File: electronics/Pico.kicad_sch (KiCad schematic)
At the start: 36 parts, among them J1 USB_B_Micro, SW1 PTS645SK50SMTR92LFS, U1 W25Q32JVZP, U2 RP2040, Y1 Crystal

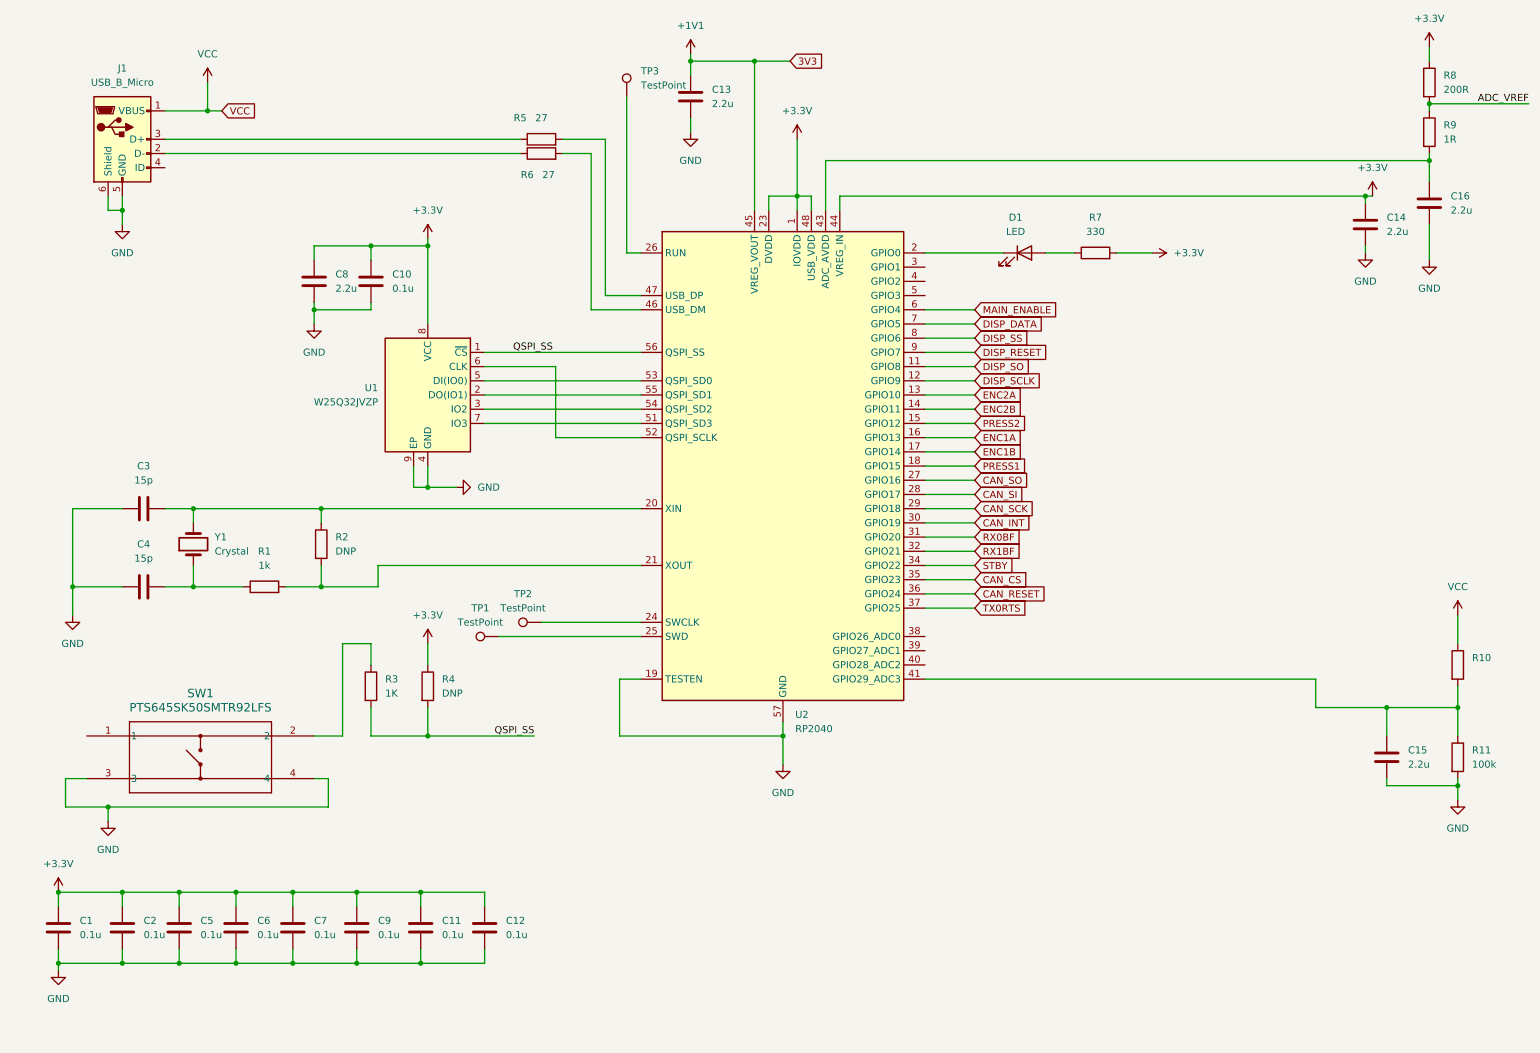
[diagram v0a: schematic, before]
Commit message: Many changes to the design. Fully routed.
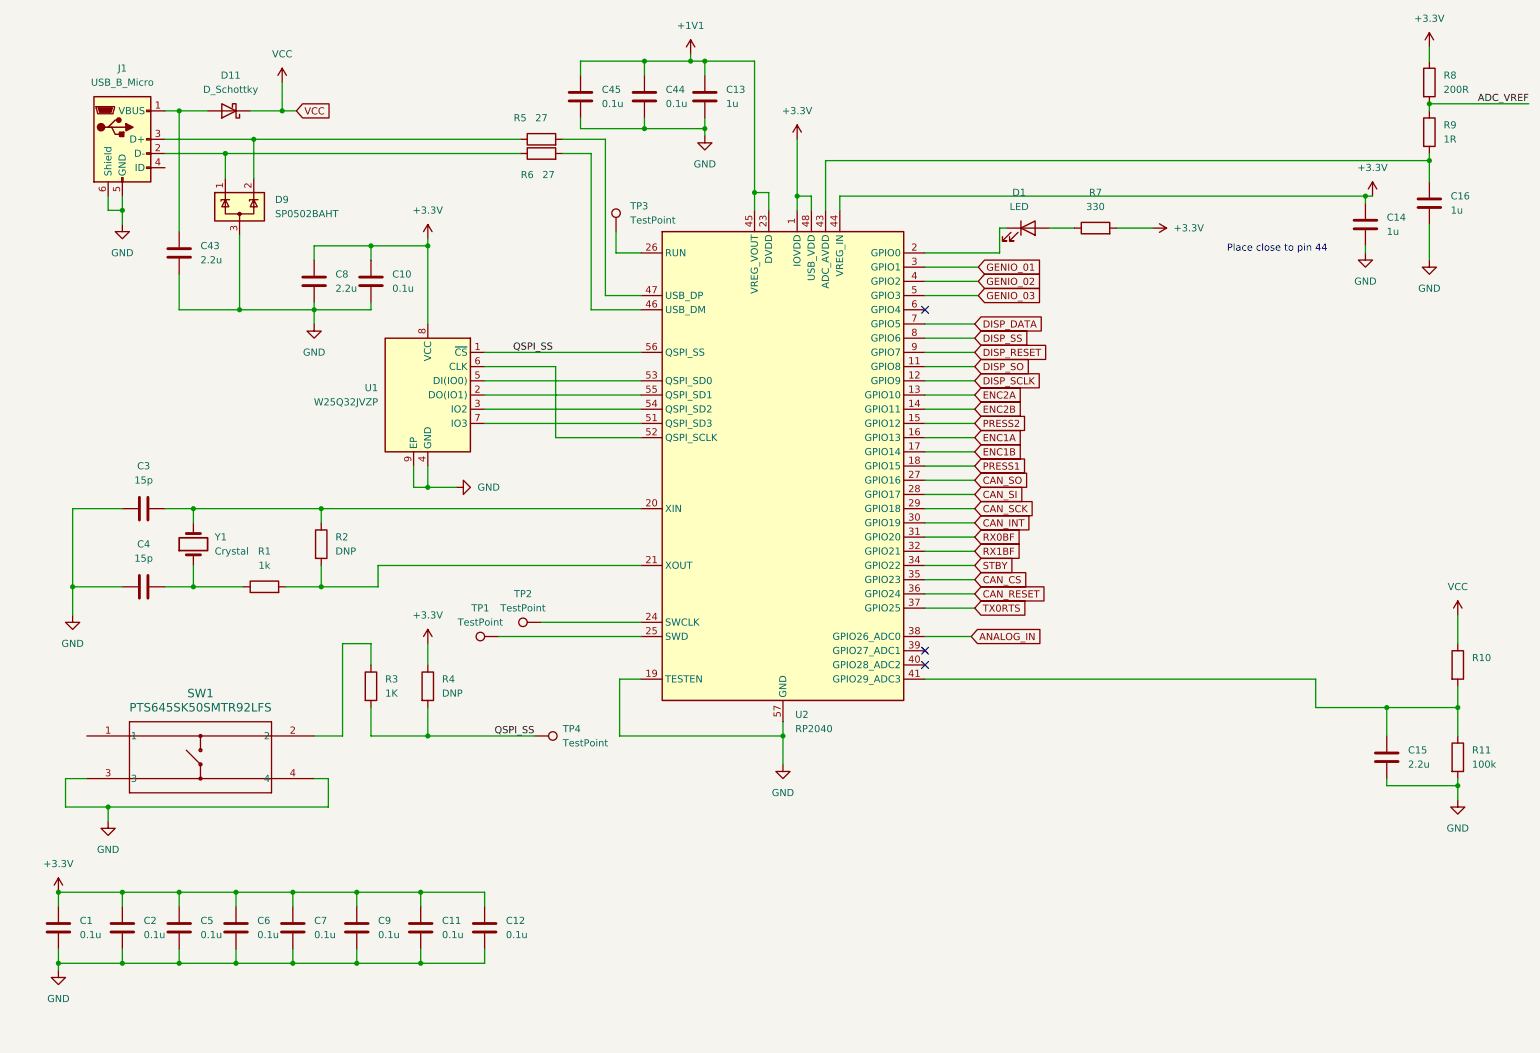
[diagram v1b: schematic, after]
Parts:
- added C43: 2.2u, Capacitor_SMD:C_0402_1005Metric, symbol Device:C
- added C44, C45: 0.1u, Capacitor_SMD:C_0402_1005Metric, symbol Device:C
- added D11: D_Schottky, Diode_SMD:D_SOD-123, symbol Device:D_Schottky
- added D9: SP0502BAHT, Package_TO_SOT_SMD:SOT-23, symbol Power_Protection:SP0502BAHT
- added TP4: TestPoint, TestPoint:TestPoint_Pad_D1.0mm, symbol Connector:TestPoint
- C1, C10, C11, C12, C15, C2, C3, C4, C5, C6, C7, C8, C9: footprint Capacitor_SMD:C_0603_1608Metric_Pad1.08x0.95mm_HandSolder -> Capacitor_SMD:C_0402_1005Metric
- C13, C14, C16: value 2.2u -> 1u; footprint Capacitor_SMD:C_0603_1608Metric_Pad1.08x0.95mm_HandSolder -> Capacitor_SMD:C_0402_1005Metric
- D1: footprint LED_SMD:LED_0603_1608Metric_Pad1.05x0.95mm_HandSolder -> LED_SMD:LED_0603_1608Metric
- R1, R10, R11, R2, R3, R4, R5, R6, R7, R8, R9: footprint Resistor_SMD:R_0603_1608Metric_Pad0.98x0.95mm_HandSolder -> Resistor_SMD:R_0402_1005Metric
- TP1: footprint Resistor_SMD:R_0603_1608Metric_Pad0.98x0.95mm_HandSolder -> TestPoint:TestPoint_Pad_D1.0mm
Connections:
- net +1V1: now also U2.23 (DVDD), U2.50 (DVDD), C44.1, C45.1
- net +3.3V: no longer U2.23 (DVDD), U2.50 (DVDD)
- net GND: now also C43.1, C44.2, C45.2, D9.3 (A)
- net QSPI_SS: now also TP4.1
- net VCC: now also D11.1 (K); no longer J1.1 (VBUS)
- net at J1.2 (D-), R6.1: now also D9.1 (K)
- net GENIO_01: now reaches U2.3 (GPIO1)
- net ANALOG_IN: now reaches U2.38 (GPIO26_ADC0)
- net GENIO_02: now reaches U2.4 (GPIO2)
- net GENIO_03: now reaches U2.5 (GPIO3)
- net at J1.3 (D+), R5.1: now also D9.2 (K)
- net MAIN_ENABLE: no longer names the net of U2.6 (GPIO4)
- new net: C43.2, D11.2 (A), J1.1 (VBUS)
- no-connect marks 0 -> 3
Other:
- note added: "Place close to pin 44"
- moved on the sheet: C13, D1, R7, TP3

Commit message: Almost sent this to fab. It is getting expensive.
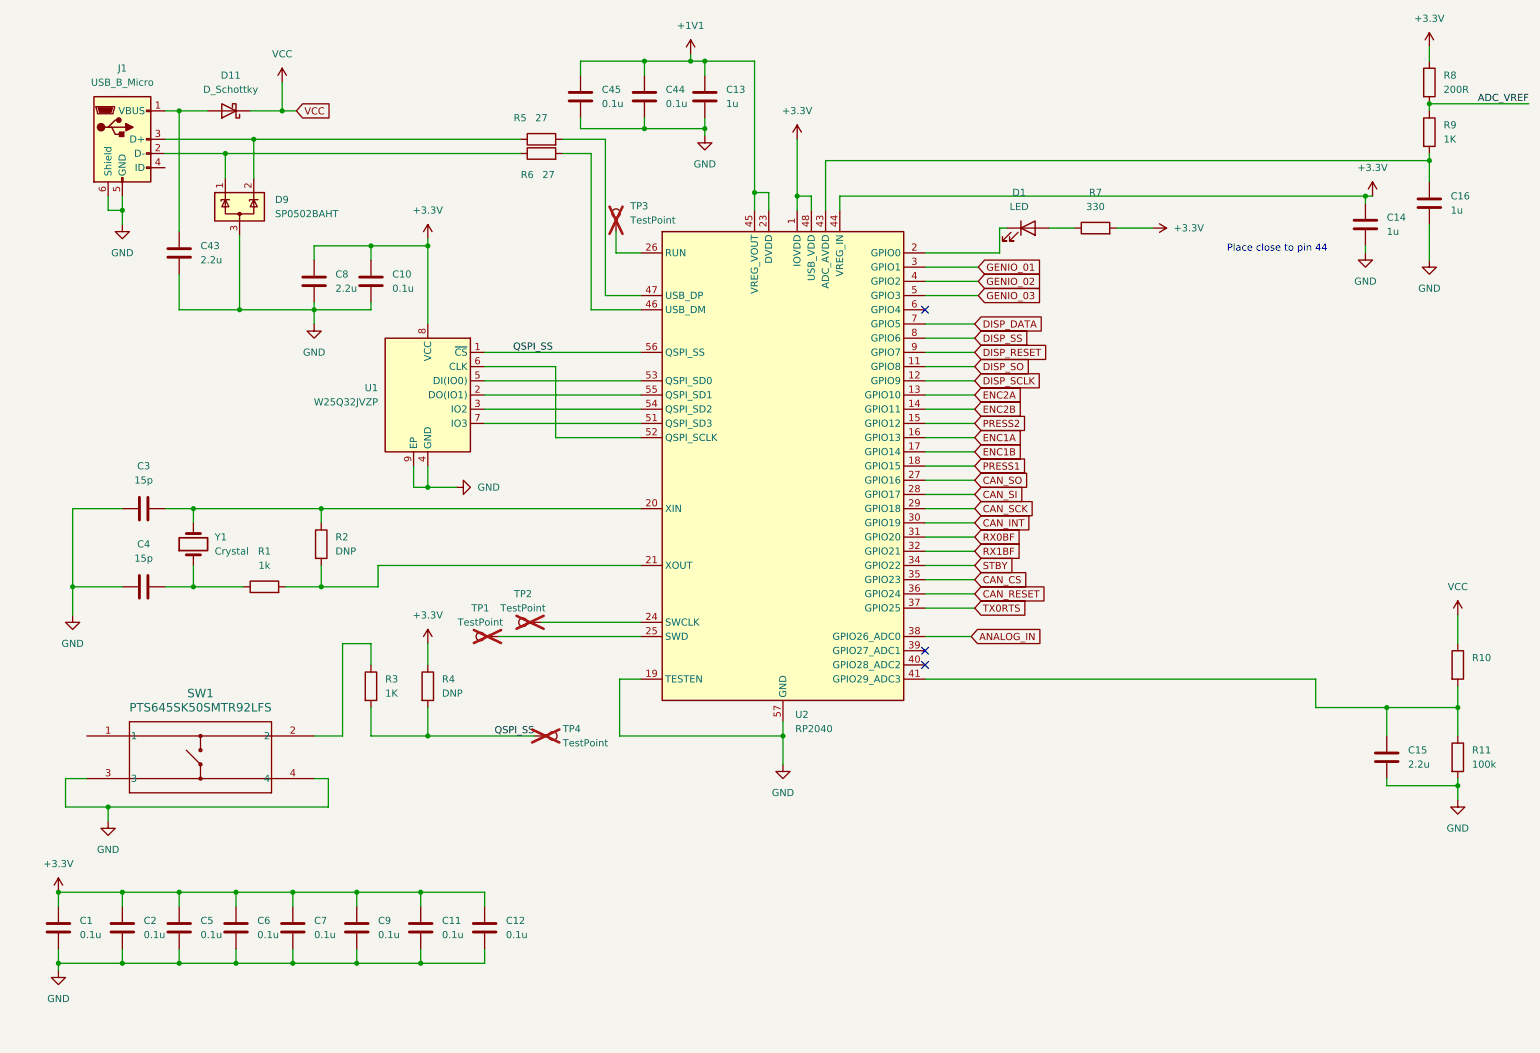
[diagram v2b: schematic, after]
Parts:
- C1, C10, C11, C12, C2, C44, C45, C5, C6, C7, C9: JLCPCB (none) -> C2655418
- D9: JLCPCB (none) -> C207261
- R1, R3: JLCPCB (none) -> C11702
- R9: value 1R -> 1K; JLCPCB (none) -> C11702
- SW1: JLCPCB (none) -> C221872
- TP1, TP2, TP3, TP4: now not fitted
- Y1: JLCPCB C90603 -> C20625731

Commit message: Switched processor.
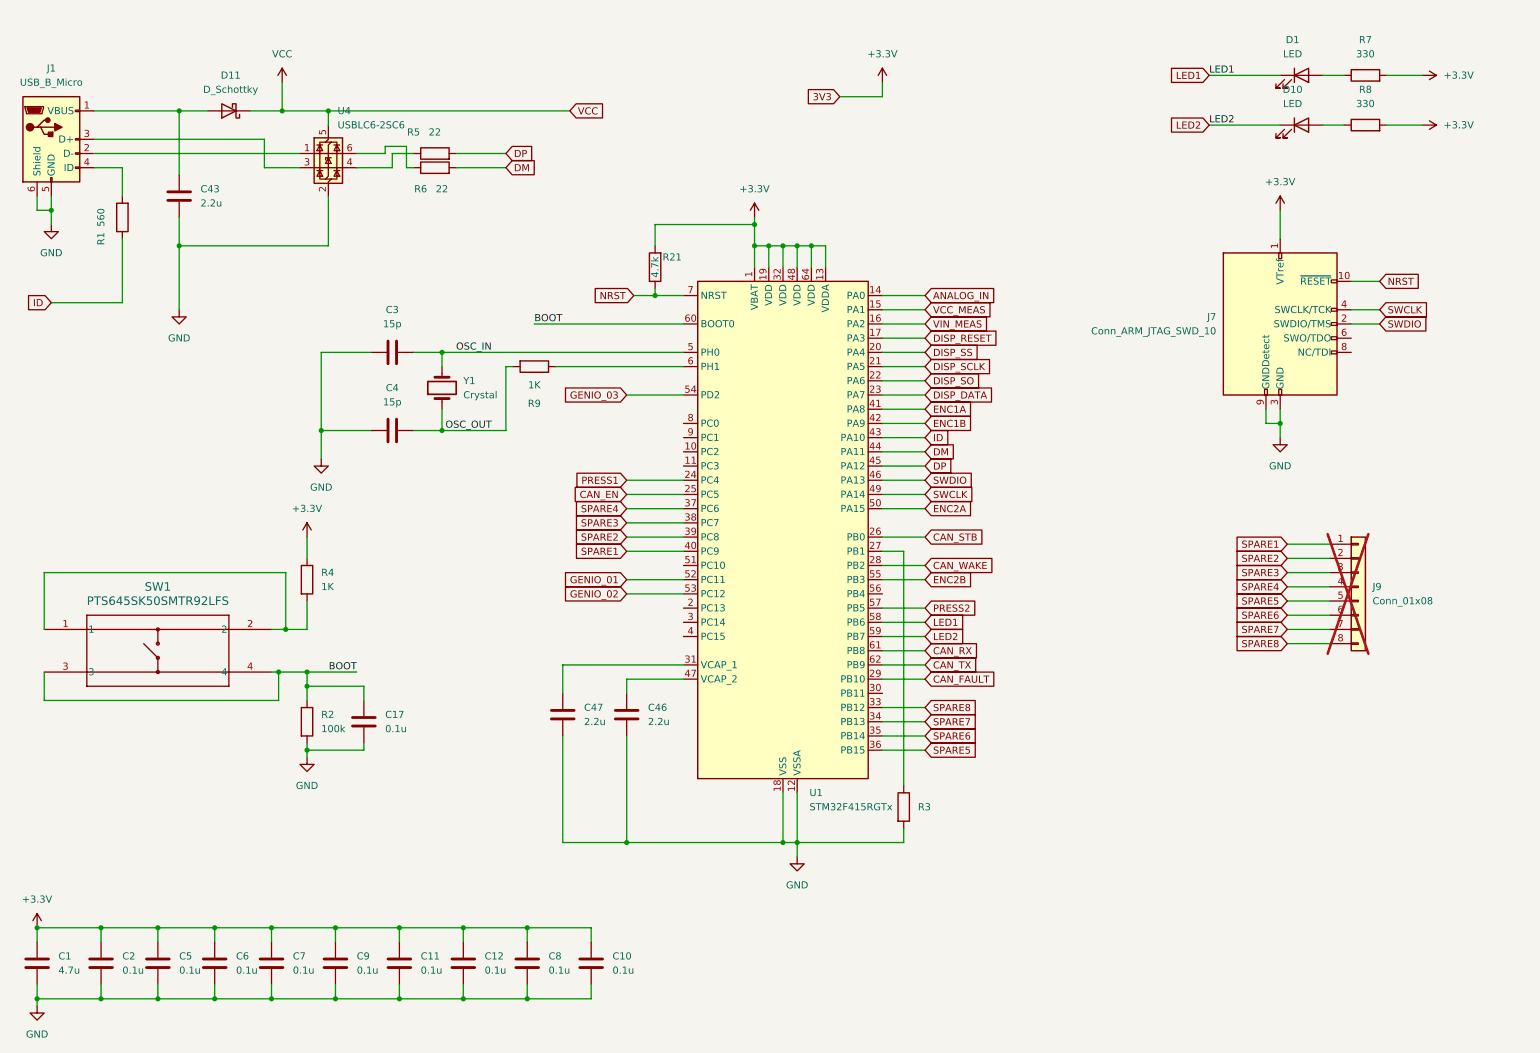
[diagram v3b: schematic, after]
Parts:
- removed C13, C14, C16: 1u, Capacitor_SMD:C_0402_1005Metric, symbol Device:C
- removed C15: 2.2u, Capacitor_SMD:C_0402_1005Metric, symbol Device:C
- removed C44, C45: 0.1u, Capacitor_SMD:C_0402_1005Metric, symbol Device:C
- removed D9: SP0502BAHT, Package_TO_SOT_SMD:SOT-23, symbol Power_Protection:SP0502BAHT
- removed R10: 200k, Resistor_SMD:R_0402_1005Metric, symbol Device:R
- removed R11: 100k, Resistor_SMD:R_0402_1005Metric, symbol Device:R
- removed TP1, TP2, TP3, TP4: TestPoint, TestPoint:TestPoint_Pad_D1.0mm, symbol Connector:TestPoint
- removed U1: W25Q32JVZP, Package_SON:WSON-8-1EP_6x5mm_P1.27mm_EP3.4x4.3mm, symbol Memory_Flash:W25Q32JVZP
- removed U2: RP2040, Package_DFN_QFN:QFN-56-1EP_7x7mm_P0.4mm_EP3.2x3.2mm, symbol MCU_RaspberryPi:RP2040
- added C17: 0.1u, Capacitor_SMD:C_0402_1005Metric, symbol Device:C
- added C46, C47: 2.2u, Capacitor_SMD:C_0402_1005Metric, symbol Device:C
- added D10: LED, LED_SMD:LED_0603_1608Metric, symbol Device:LED
- added J7: Conn_ARM_JTAG_SWD_10, Connector:Tag-Connect_TC2050-IDC-NL_2x05_P1.27mm_Vertical_with_bottom_clip, symbol Connector:Conn_ARM_JTAG_SWD_10
- added J9: Conn_01x08, Connector_PinSocket_2.54mm:PinSocket_1x08_P2.54mm_Vertical, symbol Connector_Generic:Conn_01x08
- added R21: 4.7k, Resistor_SMD:R_0402_1005Metric, symbol Device:R
- added U1: STM32F415RGTx, Package_QFP:LQFP-64_10x10mm_P0.5mm, symbol MCU_ST_STM32F4:STM32F415RGTx
- added U4: USBLC6-2SC6, Package_TO_SOT_SMD:SOT-23-6, symbol Power_Protection:USBLC6-2SC6
- C1: value 0.1u -> 4.7u
- C8: value 2.2u -> 0.1u; JLCPCB (none) -> C2655418
- R1: value 1k -> 560; JLCPCB C11702 -> (none)
- R2: value DNP -> 100k
- R3: value 1K -> 100k; JLCPCB C11702 -> (none)
- R4: value DNP -> 1K
- R5, R6: value 27 -> 22
- R8: value 200R -> 330
- R9: JLCPCB C11702 -> (none)
- Y1: JLCPCB C20625731 -> C882606
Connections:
- net +3.3V: now also R8.2, J7.1 (VTref), R21.2, U1.1 (VBAT), U1.13 (VDDA), U1.19 (VDD), U1.32 (VDD), U1.48 (VDD), U1.64 (VDD); no longer R8.1
- net ANALOG_IN: now also U1.14 (PA0)
- net DISP_DATA: now also U1.23 (PA7)
- net DISP_RESET: now also U1.17 (PA3)
- net DISP_SCLK: now also U1.21 (PA5)
- net DISP_SO: now also U1.22 (PA6)
- net DISP_SS: now also U1.20 (PA4)
- net ENC1A: now also U1.41 (PA8)
- net ENC1B: now also U1.42 (PA9)
- net ENC2A: now also U1.50 (PA15)
- net ENC2B: now also U1.55 (PB3)
- net GENIO_01: now also U1.52 (PC11)
- net GENIO_02: now also U1.53 (PC12)
- net GENIO_03: now also U1.54 (PD2)
- net GND: now also R2.2, R3.2, C17.2, C46.2, C47.2, J7.3 (GND), J7.5 (GND), J7.9 (GNDDetect), U1.12 (VSSA), U1.18 (VSS), U1.63 (VSS), U4.2 (GND); no longer SW1.3, SW1.4
- net PRESS1: now also U1.24 (PC4)
- net PRESS2: now also U1.57 (PB5)
- net VCC: now also U4.5 (VBUS)
- net OSC_OUT: now reaches C4.2, Y1.1
- net OSC_OUT: now also R9.2; no longer R1.1
- net at R1.2: now also J1.4 (ID); no longer R2.2
- net at R6.1: now also U4.6 (I/O1); no longer J1.2 (D-)
- net DM: now reaches R6.2
- net DM: now also U1.44 (PA11)
- net LED1: now reaches D1.1 (K)
- net LED1: now also U1.58 (PB6)
- net OSC_IN: now reaches C3.2, Y1.2
- net OSC_IN: now also U1.5 (PH0); no longer R2.1
- net DP: now reaches R5.2
- net DP: now also U1.45 (PA12)
- net at J1.3 (D+): now also U4.3 (I/O2); no longer R5.1
- net at SW1.1: now also R4.2, SW1.2
- net at R3.1: now also U1.27 (PB1); no longer SW1.2
- net ADC_VREF: no longer names the net of R9.1
- net ADC_VREF: now also U1.6 (PH1); no longer R8.2
- removed net QSPI_SS: R3.2, R4.2
- new net: D10.2 (A), R8.1
- new net: J1.2 (D-), U4.1 (I/O1)
- new net: R5.1, U4.4 (I/O2)
- new net: C46.1, U1.47 (VCAP_2)
- new net: C47.1, U1.31 (VCAP_1)
- new net BOOT: C17.1, R2.1, SW1.3, SW1.4, U1.60 (BOOT0)
- new net CAN_EN: U1.25 (PC5)
- new net CAN_FAULT: U1.29 (PB10)
- new net CAN_RX: U1.61 (PB8)
- new net CAN_STB: U1.26 (PB0)
- new net CAN_TX: U1.62 (PB9)
- new net CAN_WAKE: U1.28 (PB2)
- new net ID: R1.1, U1.43 (PA10)
- new net LED2: D10.1 (K), U1.59 (PB7)
- new net NRST: J7.10 (~{RESET}), R21.1, U1.7 (NRST)
- new net SPARE1: J9.1 (Pin_1), U1.40 (PC9)
- new net SPARE2: J9.2 (Pin_2), U1.39 (PC8)
- new net SPARE3: J9.3 (Pin_3), U1.38 (PC7)
- new net SPARE4: J9.4 (Pin_4), U1.37 (PC6)
- new net SPARE5: J9.5 (Pin_5), U1.36 (PB15)
- new net SPARE6: J9.6 (Pin_6), U1.35 (PB14)
- new net SPARE7: J9.7 (Pin_7), U1.34 (PB13)
- new net SPARE8: J9.8 (Pin_8), U1.33 (PB12)
- new net SWCLK: J7.4 (SWCLK/TCK), U1.49 (PA14)
- new net SWDIO: J7.2 (SWDIO/TMS), U1.46 (PA13)
- new net VCC_MEAS: U1.15 (PA1)
- new net VIN_MEAS: U1.16 (PA2)
- no-connect marks 3 -> 0
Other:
- note removed: "Place close to pin 44"
- moved on the sheet: C1, C11, C12, C2, C3, C4, C43, C5, C6, C7, C9, D1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

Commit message: Ordered this version.
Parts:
- removed Y1: Crystal, Crystal:Crystal_SMD_2520-4Pin_2.5x2.0mm, symbol Device:Crystal
- added Y2: Crystal_GND24, Crystal:Crystal_SMD_3225-4Pin_3.2x2.5mm, symbol Device:Crystal_GND24
- C1: footprint Capacitor_SMD:C_0402_1005Metric -> Capacitor_SMD:C_0805_2012Metric; JLCPCB C2655418 -> (none)
- C10, C11, C12, C17, C2, C5, C6, C7, C8, C9: JLCPCB C2655418 -> C432917
- C43: footprint Capacitor_SMD:C_0402_1005Metric -> Capacitor_SMD:C_0603_1608Metric; JLCPCB (none) -> C76612
- C46, C47: footprint Capacitor_SMD:C_0402_1005Metric -> Capacitor_SMD:C_0603_1608Metric; JLCPCB C2655418 -> C76612
- D1: JLCPCB (none) -> C2837377
- D10: JLCPCB (none) -> C84267
- D11: JLCPCB C130887 -> C7420325
- J7: now not fitted
- R1: footprint Resistor_SMD:R_0402_1005Metric -> Resistor_SMD:R_0603_1608Metric; JLCPCB (none) -> C423025
- R4, R9: JLCPCB (none) -> C11702
- U4: JLCPCB (none) -> C7519
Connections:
- net OSC_IN: now also Y2.3
- net OSC_OUT: now also Y2.1
- no-connect marks 0 -> 2
